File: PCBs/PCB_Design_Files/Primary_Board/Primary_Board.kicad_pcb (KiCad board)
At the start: 4 copper layers, 40.3 x 57.1 mm, 107 parts, among them J1 Conn_FFC_8pin, J2 Conn_01x08_Pin, U1 OPA381, U11 TMUX1104DGSR, U12 TMUX1133PWR, U13 TMUX1133PWR, U14 TMUX1133PWR, U15 TMUX1133PWR, U2 TLV9002, U4 TLV9002, U5 MOUDLE-SEEEDUINO-XIAO-ESP32C3, U6 DM-OLED096-636, U7 REF3333AIDBZR, U8 TMUX1133PWR, U9 MCP6561T-E/OT

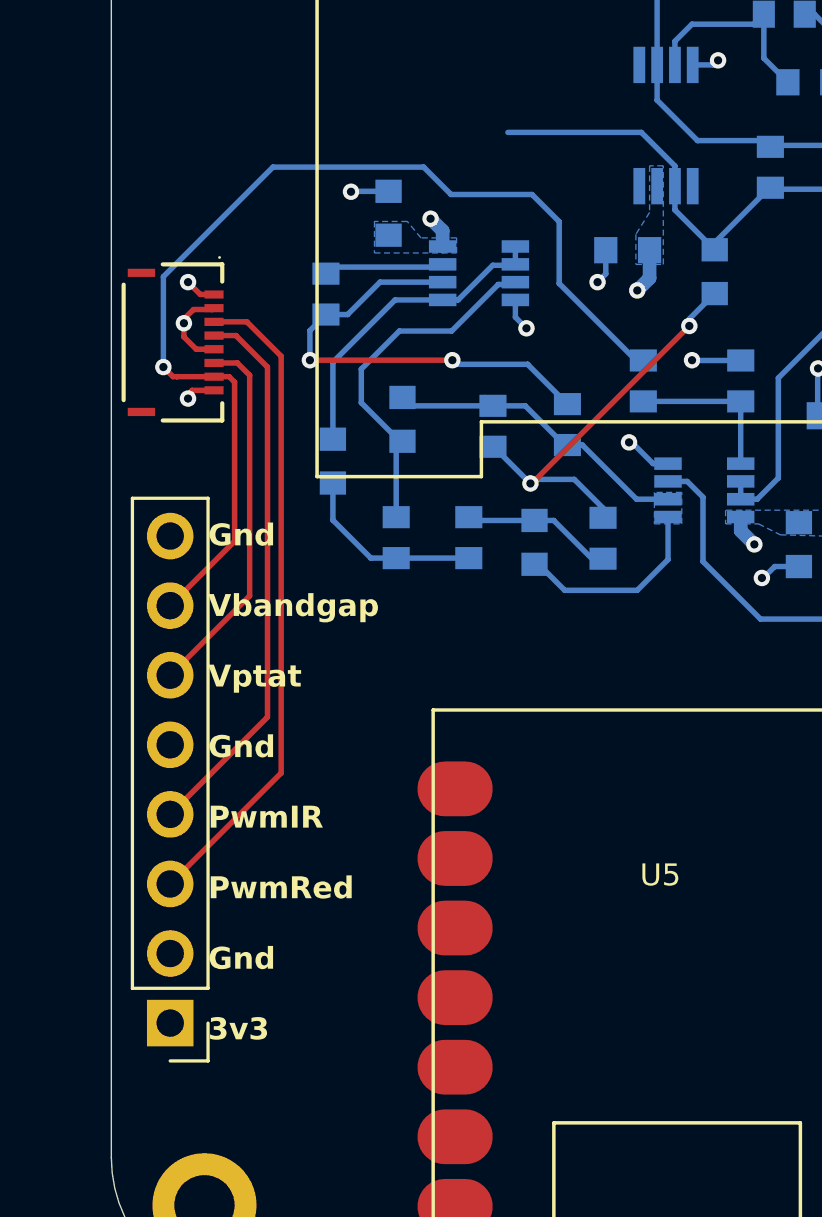
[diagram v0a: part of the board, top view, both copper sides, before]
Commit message: TH header labels
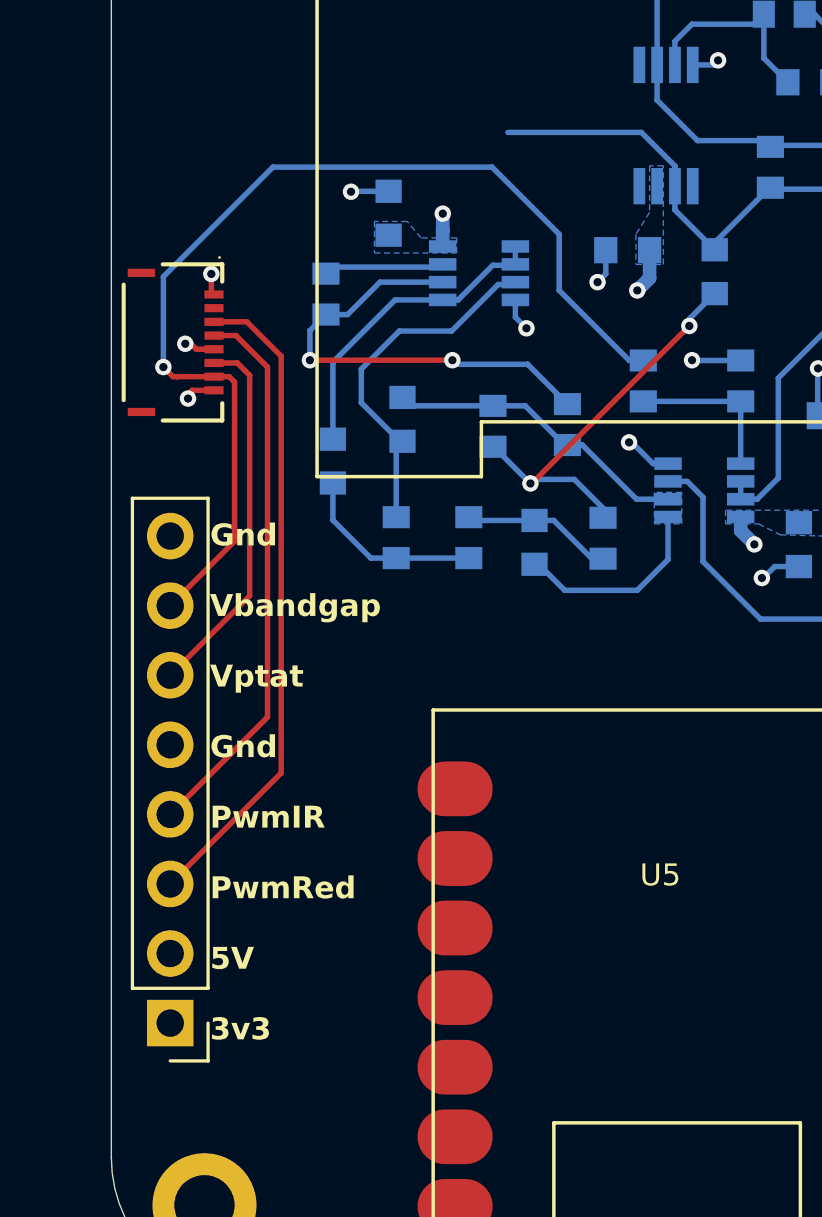
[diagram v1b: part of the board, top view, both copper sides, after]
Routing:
- net GND: track 20.1 -> 18.1 mm
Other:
- board text added: "Gnd Vbandgap Vptat Gnd PwmIR PwmRed 5V 3v3"
- board text removed: "Gnd Vbandgap Vptat Gnd PwmIR PwmRed Gnd 3v3"
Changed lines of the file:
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@@
 		(layer "Edge.Cuts")
 	)
-	(gr_text "Gnd\n\nVbandgap\n\nVptat\n\nGnd\n\nPwmIR\n\nPwmRed\n\nGnd\n\n3v3"
-		(at 129.53 121.09 0)
+	(gr_text "Gnd\n\nVbandgap\n\nVptat\n\nGnd\n\nPwmIR\n\nPwmRed\n\n5V\n\n3v3"
+		(at 129.6 121.09 0)
 		(layer "F.SilkS")
 		(effects
@@
 	)
 	(segment
-		(start 129.699998 94.35)
-		(end 129.75 94.299998)
-		(width 0.2)
-		(layer "F.Cu")
-		(net 2)
-	)
-	(segment
-		(start 129 94.35)
-		(end 129.699998 94.35)
-		(width 0.2)
-		(layer "F.Cu")
-		(net 2)
-	)
-	(segment
-		(start 128.65 94.85)
-		(end 128.65 95.35)
-		(width 0.2)
-		(layer "F.Cu")
-		(net 2)
-	)
-	(segment
-		(start 128.65 94.85)
-		(end 128.65 94.7)
+		(start 128.9 95.6)
+		(end 129.1 95.8)
+		(width 0.2)
+		(layer "F.Cu")
+		(net 2)
+	)
+	(segment
+		(start 128.7 95.6)
+		(end 128.9 95.6)
 		(width 0.2)
 		(layer "F.Cu")
@@
 	)
 	(segment
-		(start 128.65 94.7)
-		(end 129 94.35)
-		(width 0.2)
-		(layer "F.Cu")
-		(net 2)
-	)
-	(segment
 		(start 128.8 97.6)
 		(end 128.8 97.45)
@@
 	)
 	(segment
-		(start 128.65 95.35)
-		(end 129.1 95.8)
-		(width 0.2)
-		(layer "F.Cu")
-		(net 2)
-	)
-	(segment
 		(start 129.85 95.8)
 		(end 129.45 95.8)
@@
 		(net 2)
 	)
-	(via
-		(at 128.65 94.85)
+	(segment
+		(start 128.7 95.6)
+		(end 128.65 95.55)
+		(width 0.2)
+		(layer "F.Cu")
+		(net 2)
+	)
+	(via
+		(at 128.7 95.6)
 		(size 0.6)
 		(drill 0.3)
@@
 	)
 	(segment
-		(start 129.75 93.799999)
-		(end 129.249999 93.799999)
+		(start 129.65 93.699999)
+		(end 129.75 93.799999)
 		(width 0.2)
 		(layer "F.Cu")
@@
 	)
 	(segment
-		(start 129.249999 93.799999)
-		(end 128.8 93.35)
+		(start 129.65 93.05)
+		(end 129.65 93.699999)
 		(width 0.2)
 		(layer "F.Cu")
@@
 	)
 	(via
-		(at 137.65505 91.034993)
+		(at 138.1 90.85)
 		(size 0.6)
 		(drill 0.3)
@@
 	)
 	(via
-		(at 128.8 93.35)
+		(at 129.65 93.05)
 		(size 0.6)
 		(drill 0.3)
@@
 		(drill 0.3)
 		(layers "F.Cu" "B.Cu")
+		(net 4)
+	)
+	(segment
+		(start 138.0957 91.475643)
+		(end 138.0957 92.050014)
+		(width 0.5)
+		(layer "B.Cu")
 		(net 4)
 	)
@@
 	)
 	(segment
-		(start 138.0957 91.475643)
-		(end 137.65505 91.034993)
+		(start 138.1 90.85)
+		(end 138.1 91.471343)
 		(width 0.5)
 		(layer "B.Cu")
@@
 	)
 	(segment
+		(start 138.1 91.471343)
+		(end 138.0957 91.475643)
+		(width 0.5)
+		(layer "B.Cu")
+		(net 4)
+	)
+	(segment
 		(start 145.65 93.203571)
 		(end 145.2 93.653571)
@@
 	)
 	(segment
-		(start 138.0957 92.050014)
-		(end 138.0957 91.475643)
-		(width 0.5)
-		(layer "B.Cu")
-		(net 4)
-	)
-	(segment
 		(start 141.425 100.625)
 		(end 147.1 94.95)
@@
 	)
 	(segment
-		(start 141.358866 90.15)
-		(end 142.35 91.141134)
+		(start 144.910093 96.210093)
+		(end 145.42115 96.210093)
+		(width 0.2)
+		(layer "B.Cu")
+		(net 40)
+	)
+	(segment
+		(start 139.9 89.15)
+		(end 142.35 91.6)
+		(width 0.2)
+		(layer "B.Cu")
+		(net 40)
+	)
+	(segment
+		(start 142.35 93.65)
+		(end 144.910093 96.210093)
+		(width 0.2)
+		(layer "B.Cu")
+		(net 40)
+	)
+	(segment
+		(start 142.35 91.6)
+		(end 142.35 93.65)
+		(width 0.2)
+		(layer "B.Cu")
+		(net 40)
+	)
+	(segment
+		(start 131.9 89.15)
+		(end 139.9 89.15)
 		(width 0.2)
 		(layer "B.Cu")
@@
 	)
 	(segment
-		(start 137.4 89.15)
-		(end 138.4 90.15)
-		(width 0.2)
-		(layer "B.Cu")
-		(net 40)
-	)
-	(segment
 		(start 127.9 96.45)
 		(end 127.9 93.15)
@@
 	)
 	(segment
-		(start 131.9 89.15)
-		(end 137.4 89.15)
-		(width 0.2)
-		(layer "B.Cu")
-		(net 40)
-	)
-	(segment
-		(start 138.4 90.15)
-		(end 141.358866 90.15)
-		(width 0.2)
-		(layer "B.Cu")
-		(net 40)
-	)
-	(segment
-		(start 142.35 91.141134)
-		(end 142.35 93.4)
-		(width 0.2)
-		(layer "B.Cu")
-		(net 40)
-	)
-	(segment
-		(start 142.35 93.4)
-		(end 145.160093 96.210093)
-		(width 0.2)
-		(layer "B.Cu")
-		(net 40)
-	)
-	(segment
-		(start 145.160093 96.210093)
-		(end 145.42115 96.210093)
-		(width 0.2)
-		(layer "B.Cu")
-		(net 40)
-	)
-	(segment
 		(start 131.7 109.23)
 		(end 128.15 112.78)
@@
 	)
 	(segment
+		(start 129.699998 94.35)
+		(end 129.75 94.299998)
+		(width 0.2)
+		(layer "F.Cu")
+		(net 67)
+	)
+	(segment

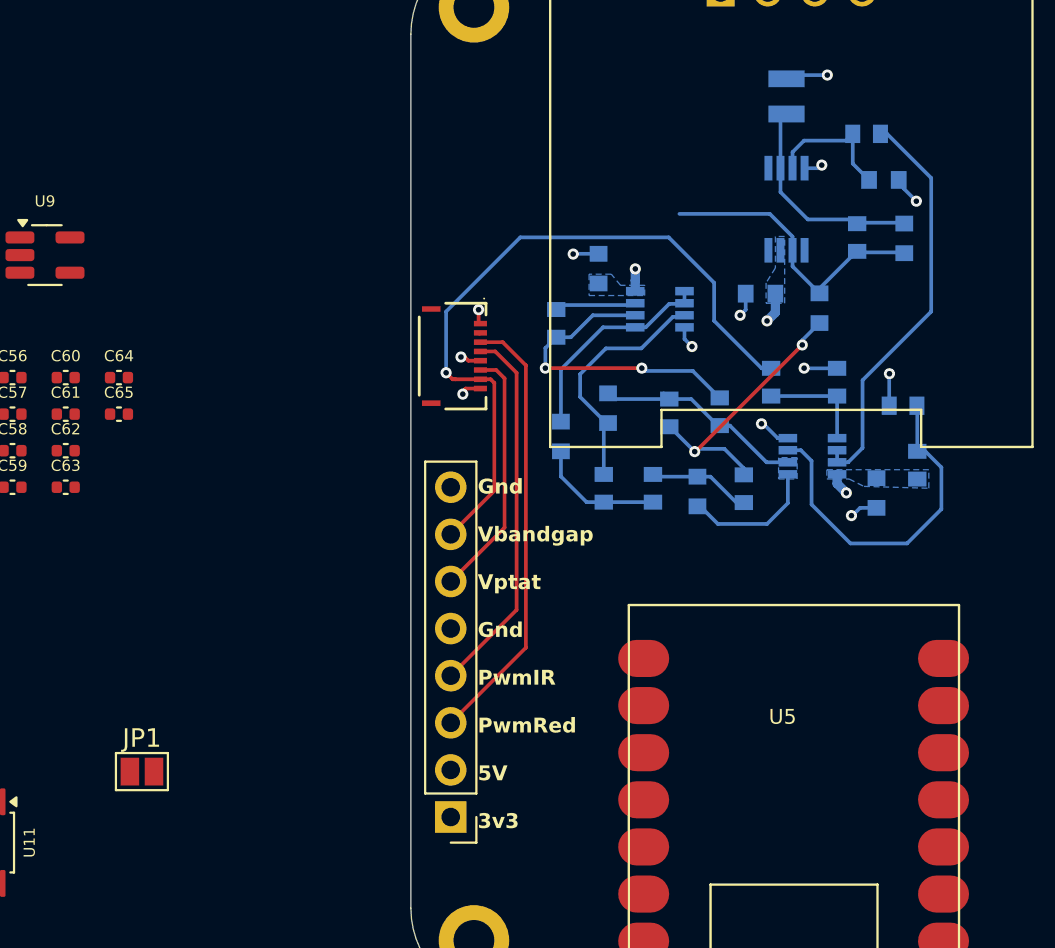
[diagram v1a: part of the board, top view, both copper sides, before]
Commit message: Added symbols for Voltage Search DAC
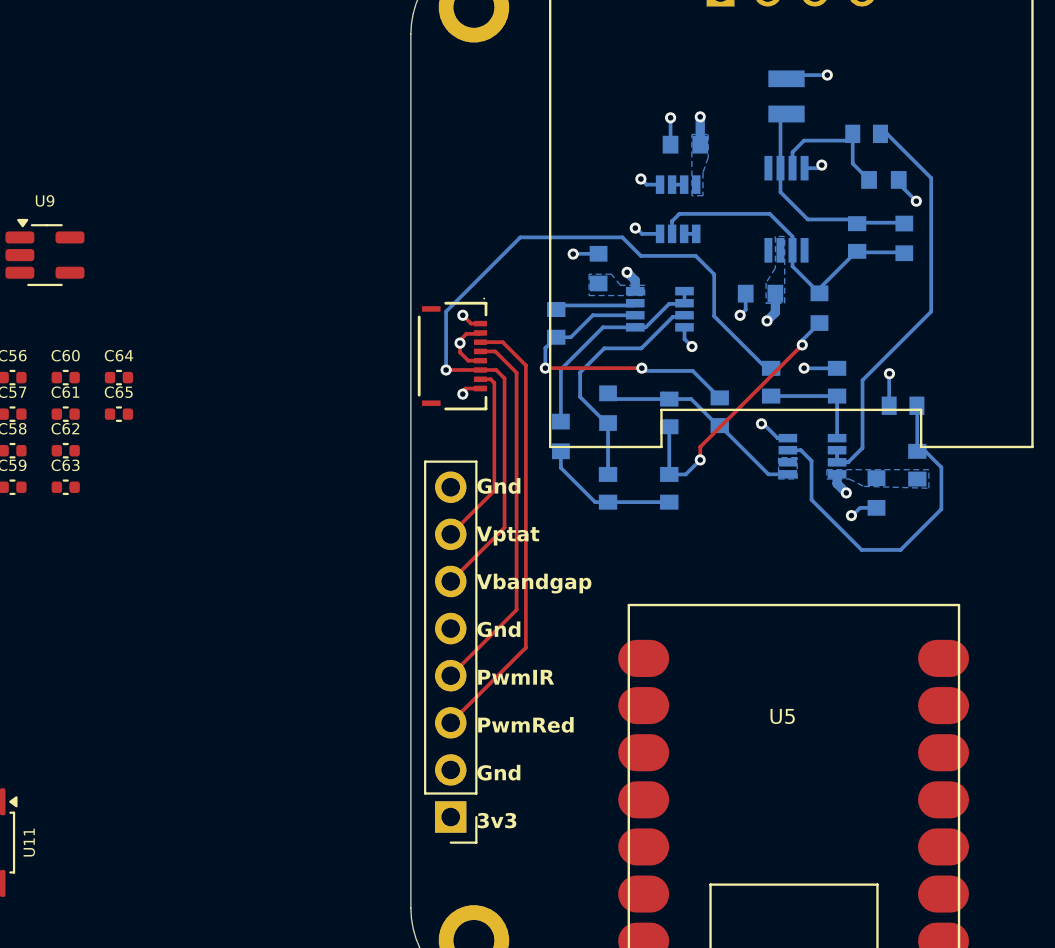
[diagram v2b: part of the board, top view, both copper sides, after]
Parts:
- removed C68: 220n, Project Footprints:0603_capacitor
- removed JP1: ADC_BYPASS, Jumper:SolderJumper-2_P1.3mm_Open_Pad1.0x1.5mm
- removed R17: 100k, Project Footprints:0603_resistor
- added C4: .1u, Project Footprints:0603_capacitor, B.Cu at (140.8, 84.2)
- added U3: TLV9002, Project Footprints:TLV9002, B.Cu at (140.4, 87.6)
- R10: value 40k -> 35k
- R4, R5: value 100k -> 120k
- moved R4 0.88 mm to (139.9, 102.7)
- moved R5 0.23 mm to (136.6, 102.7)
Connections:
- C2 pad 2: /AFE/TIA_OUT -> /AFE/TIA_Out
- C5 pad 1: /AFE/TIA_OUT -> /AFE/TIA_Out
- J1 pad 6: /V_ptat -> /V_bandgap
- J1 pad 7: /V_bandgap -> /V_ptat
- J2 pad 6: /V_ptat -> /V_bandgap
- J2 pad 7: /V_bandgap -> /V_ptat
- R13 pad 1: /AFE/TIA_OUT -> /ADC/ADC_Input2
- R2 pad 2: /AFE/TIA_OUT -> /AFE/TIA_Out
- R4 pad 1: Net-(C68-Pad1) -> Net-(C5-Pad2)
- U1 pad 6: /AFE/TIA_OUT -> /AFE/TIA_Out
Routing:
- net /AFE/TIA_Out: track 0.00 -> 17.2 mm
- net /AFE/TIA_OUT: track 16.0 -> 0.00 mm
- net /AFE/+1.65V: track 19.1 -> 12.0 mm
- net GND: track 18.1 -> 24.2 mm, vias 12 -> 15
- net Net-(C68-Pad1): track 5.55 -> 0.00 mm
- net /V_ptat: track 13.6 -> 9.87 mm
- net /V_bandgap: track 38.5 -> 42.1 mm
- net +3V3: track 4.86 -> 6.70 mm, vias 4 -> 5
- net Net-(C5-Pad2): track 15.4 -> 14.6 mm
- net /ADC/ADC_Input2: track 0.00 -> 0.65 mm
- net Net-(U3-IN2-): track 0.00 -> 0.65 mm
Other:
- board text added: "Gnd Vptat Vbandgap Gnd PwmIR PwmRed Gnd 3v3"
- board text removed: "Gnd Vbandgap Vptat Gnd PwmIR PwmRed 5V 3v3"

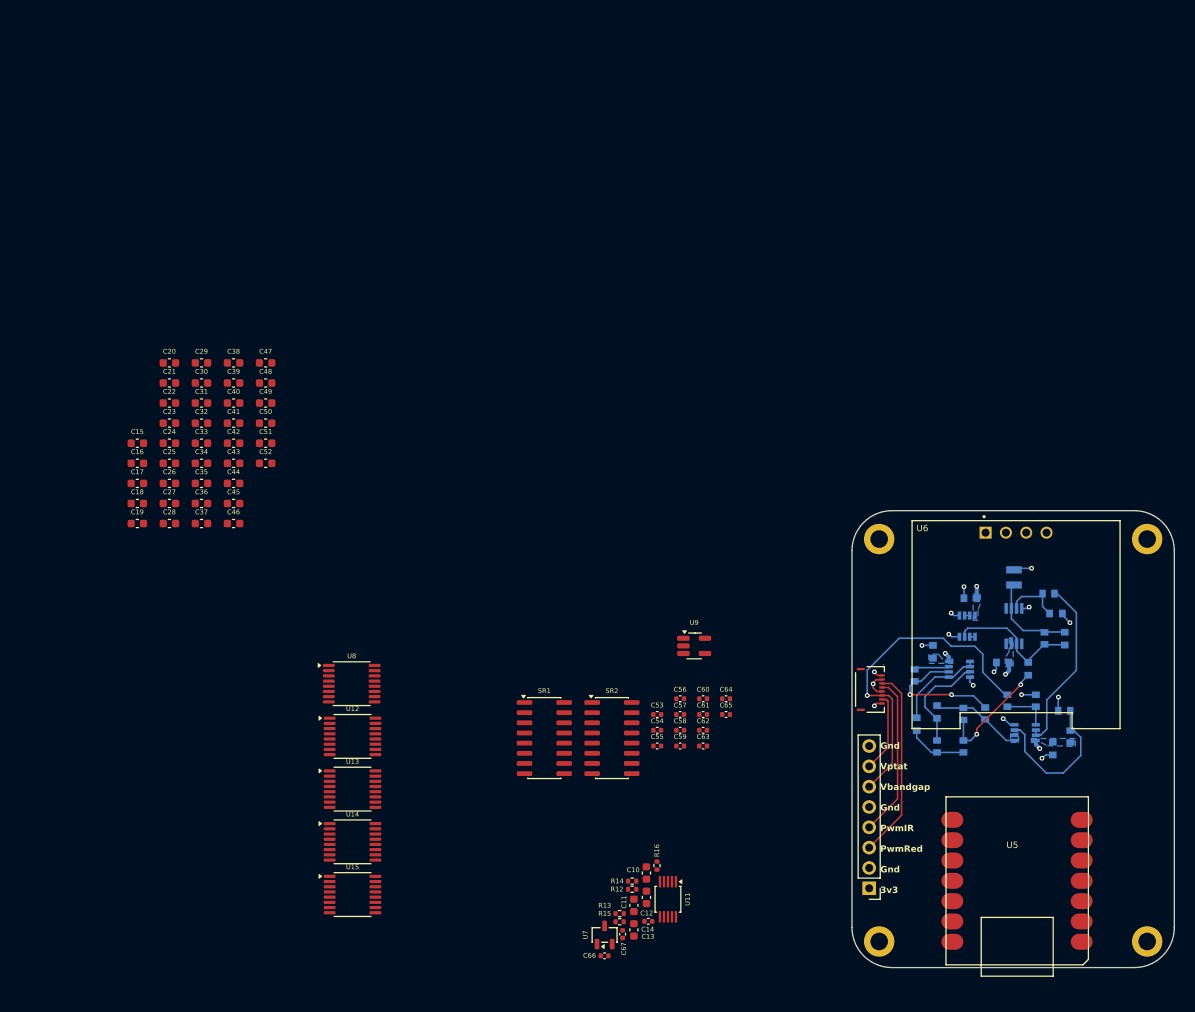
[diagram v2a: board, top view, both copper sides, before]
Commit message: Added Voltage Search DAC
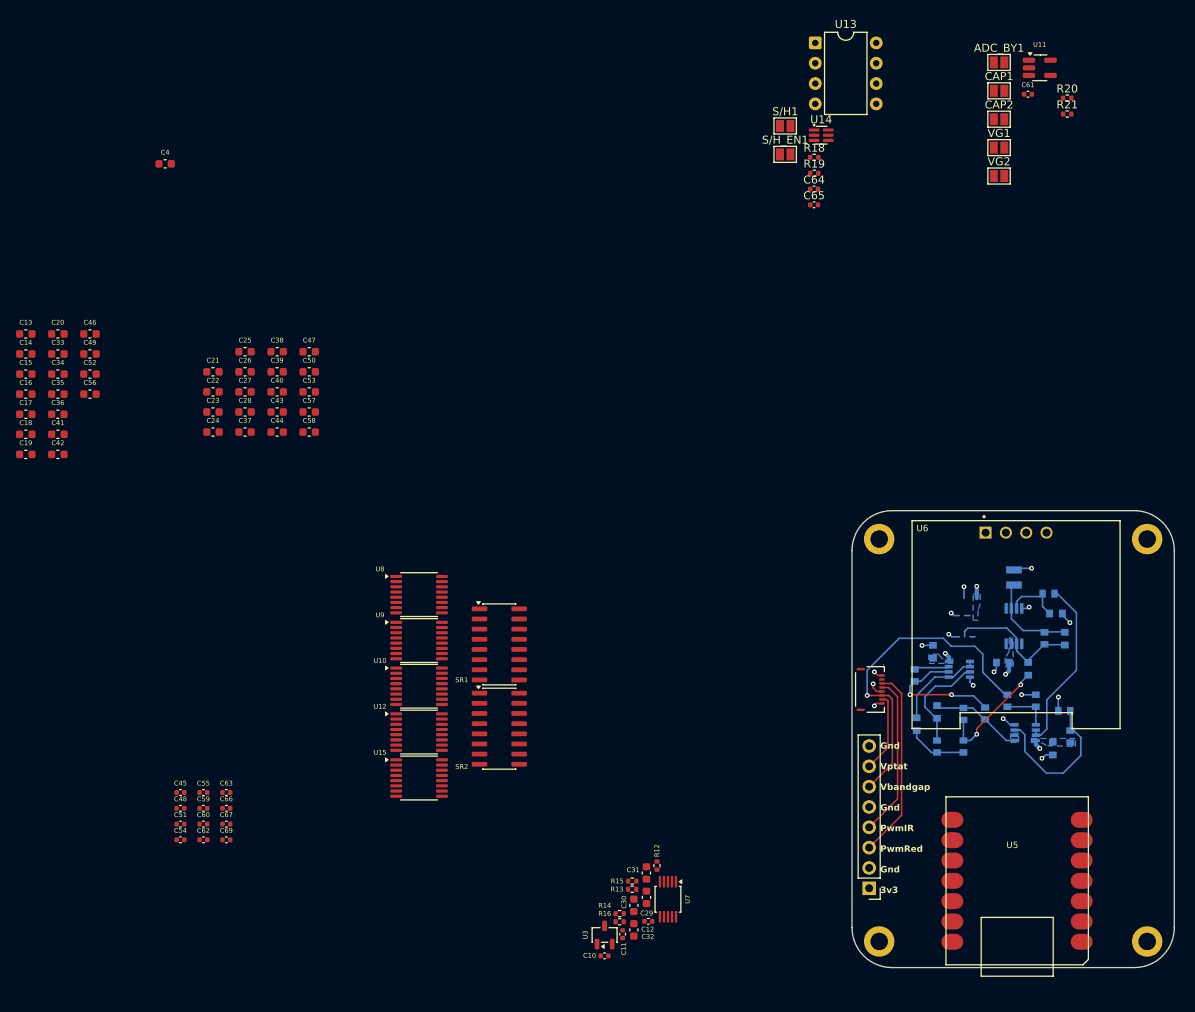
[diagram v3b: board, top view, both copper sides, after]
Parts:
- removed the C4 at (140.8, 84.2)
- removed the U3 at (140.4, 87.6)
- added ADC_BY1: ADC_BYPASS, Jumper:SolderJumper-2_P1.3mm_Open_Pad1.0x1.5mm, F.Cu at (144.4, 17.2)
- added C64: 100nF, Capacitor_SMD:C_0402_1005Metric, F.Cu at (121.3, 33.0)
- added C65: 1nF, Capacitor_SMD:C_0402_1005Metric, F.Cu at (121.3, 35.0)
- added CAP1: CAP, Jumper:SolderJumper-2_P1.3mm_Open_Pad1.0x1.5mm, F.Cu at (144.4, 20.7)
- added CAP2: CAP, Jumper:SolderJumper-2_P1.3mm_Open_Pad1.0x1.5mm, F.Cu at (144.4, 24.3)
- added R18: 1k, Resistor_SMD:R_0402_1005Metric, F.Cu at (121.3, 29.0)
- added R19: 1k, Resistor_SMD:R_0402_1005Metric, F.Cu at (121.3, 31.0)
- added R20: 10k, Resistor_SMD:R_0402_1005Metric, F.Cu at (152.9, 21.6)
- added R21: 10k, Resistor_SMD:R_0402_1005Metric, F.Cu at (152.9, 23.6)
- added S/H1: TVG, Jumper:SolderJumper-2_P1.3mm_Open_Pad1.0x1.5mm, F.Cu at (117.7, 25.1)
- added S/H_EN1: TVG, Jumper:SolderJumper-2_P1.3mm_Open_Pad1.0x1.5mm, F.Cu at (117.7, 28.7)
- added U13: LF398N/NOPB, Package_DIP:DIP-8_W7.62mm, F.Cu at (121.4, 14.7)
- added U14: AD5621AKSZ, Package_TO_SOT_SMD:SOT-363_SC-70-6, F.Cu at (122.2, 26.3)
- added VG1: TVG, Jumper:SolderJumper-2_P1.3mm_Open_Pad1.0x1.5mm, F.Cu at (144.4, 27.8)
- added VG2: TVG, Jumper:SolderJumper-2_P1.3mm_Open_Pad1.0x1.5mm, F.Cu at (144.4, 31.4)
- R10: value 35k -> 40k
- R4, R5: value 120k -> 100k
- moved C61 86.2 mm to (148.0, 21.1)
- moved U11 84.2 mm to (149.5, 17.8)
- moved C45 66.4 mm to (42.1, 108.4)
- moved C67 64.4 mm to (47.8, 112.4)
- moved C60 63.6 mm to (44.9, 112.4)
- moved C55 63.2 mm to (44.9, 108.4)
- moved C62 61.6 mm to (44.9, 114.3)
- moved C59 61.1 mm to (44.9, 110.4)
- moved C54 61.1 mm to (42.1, 114.3)
- moved C48 60.7 mm to (42.1, 110.4)
- moved C51 60.4 mm to (42.1, 112.4)
- moved C63 59.9 mm to (47.8, 108.4)
- moved C69 57.9 mm to (47.8, 114.3)
- moved C66 57.6 mm to (47.8, 110.4)
- moved C4 37.1 mm to (40.1, 29.8)
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- renumbered C66 to C10, C67 to C11, C14 to C12, C15 to C13, C16 to C14, C17 to C15, C18 to C16, C19 to C17, C20 to C18, C21 to C19, C22 to C20, C33 to C21, C34 to C22, C35 to C23, C36 to C24, C37 to C25, C38 to C26, C39 to C27, C40 to C28, C12 to C29, C11 to C30, C10 to C31, C13 to C32, C23 to C33, C24 to C34, C25 to C35, C26 to C36, C41 to C37, C42 to C38, C43 to C39, C51 to C4, C44 to C40, C27 to C41, C28 to C42, C45 to C43, C46 to C44, C60 to C45, C29 to C46, C53 to C48, C30 to C49, C48 to C50, C55 to C51, C31 to C52, C49 to C53, C61 to C55, C32 to C56, C50 to C57, C52 to C58, C56 to C59, C62 to C60, C65 to C61, C57 to C62, C58 to C66, C64 to C67, C59 to C69, R16 to R12, R12 to R13, R13 to R14, R14 to R15, R15 to R16, U13 to U10, U9 to U11, U14 to U12, U7 to U3, U11 to U7, U12 to U9
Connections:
- C2 pad 2: /AFE/TIA_Out -> /AFE/TIA_OUT
- C5 pad 1: /AFE/TIA_Out -> /AFE/TIA_OUT
- J1 pad 6: /V_bandgap -> /V_ptat
- J1 pad 7: /V_ptat -> /V_bandgap
- J2 pad 6: /V_bandgap -> /V_ptat
- J2 pad 7: /V_ptat -> /V_bandgap
- R14 pad 1: /ADC/ADC_Input2 -> /AFE/TIA_OUT
- R2 pad 2: /AFE/TIA_Out -> /AFE/TIA_OUT
- R4 pad 1: Net-(C5-Pad2) -> Net-(C68-Pad1)
- U1 pad 6: /AFE/TIA_Out -> /AFE/TIA_OUT
- U11 pad 1: /ADC/V_COMP -> /ADC/ADC_OUT
- U11 pad 3: /ADC/MSB_TOP -> Net-(CAP1-B)
- U11 pad 4: /AFE/+1.65V -> Net-(CAP2-B)
- U5 pad 1: unconnected-(U5-PA02_A0_D0-Pad1) -> /ADC/ADC_OUT
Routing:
- net /AFE/TIA_Out: track 17.2 -> 0.00 mm
- net /AFE/TIA_OUT: track 0.00 -> 17.2 mm
- net /V_ptat: track 9.87 -> 0.00 mm
- net /V_bandgap: track 42.1 -> 51.9 mm
- net (no net): track 0.00 -> 1.30 mm
- net GND: track 24.2 -> 22.9 mm
- net /ADC/ADC_Input2: track 0.65 -> 0.00 mm
- net Net-(U3-IN2-): track 0.65 -> 0.00 mm
